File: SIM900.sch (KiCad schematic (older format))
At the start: 72 parts, among them J1 Conn_01x05, J11 Conn_Coaxial_Power, J12 AudioJack2_Ground, J13 AudioJack2_Ground, J2 Conn_01x04, J3 Conn_01x04, J4 Conn_01x06, J5 Conn_01x02, J6 Conn_01x06, J7 Conn_01x03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

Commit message: Se realizaron los cambios a los comentarios hechos por el profesor
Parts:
- C1, C10, C11, C12, C13, C14, C15, C16, C17, C18, C19, C2, C20, C3, C4, C5, C6, C7, C8: Digikey (none) -> 399-17617-2-ND
- C9: Degikey (none) -> 399-17617-2-ND
- D1, D11, D2, D4: Digikey (none) -> SMAJ22CAQ-13-FDITR-ND
- D10, D8, D9: Digikey (none) -> BZD27C16P-E3-08GITR-ND
- D3: Digikey (none) -> 2460-L171L-QYC-TR-ND
- D5: Digokey (none) -> SMAJ22CAQ-13-FDITR-ND
- D6: Digikey (none) -> 2460-L171L-LICTR-ND
- D7: Field4 (none) -> BZD27C16P-E3-08GITR-ND
- J1: Digikey (none) -> S6103-ND
- J11: Digikey (none) -> H9161DKR-ND
- J12, J13: Digikey (none) -> CP-SJ2-35813B-SMT-DKR-ND
- J2, J3: Digikey (none) -> S9009E-04-ND
- J4, J6: Digikey (none) -> S7004-ND
- J7: Digikey (none) -> S9008E-03-ND
- J8: Digikey (none) -> 2057-RF2-49B-T-00-50-G-HDW-ND
- J9: Digikey (none) -> WM6698DKR-ND
- L1: footprint Inductor_SMD:L_0603_1608Metric_Pad1.05x0.95mm_HandSolder -> Inductor_SMD:L_0805_2012Metric; Digikey (none) -> 490-LQW2BAS6N0J00LDKR-ND
- Q1, Q2, Q3: Digikey (none) -> BC848BHZGT116DKR-ND
- R1, R10, R11, R12, R13, R15, R2, R3, R4, R5, R6, R7, R8: Digikey (none) -> 73L3R10JTR-ND
- R9: Degikey (none) -> 73L3R10JTR-ND
- U1: Digikey (none) -> 576-1124-ND
- U2: Digikey (none) -> 1597-1231-ND
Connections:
- net RXD: now also XA1.25 (rs232TXD); no longer XA1.23 (rs232RXD)
- net TXD: now also XA1.23 (rs232RXD); no longer XA1.25 (rs232TXD)

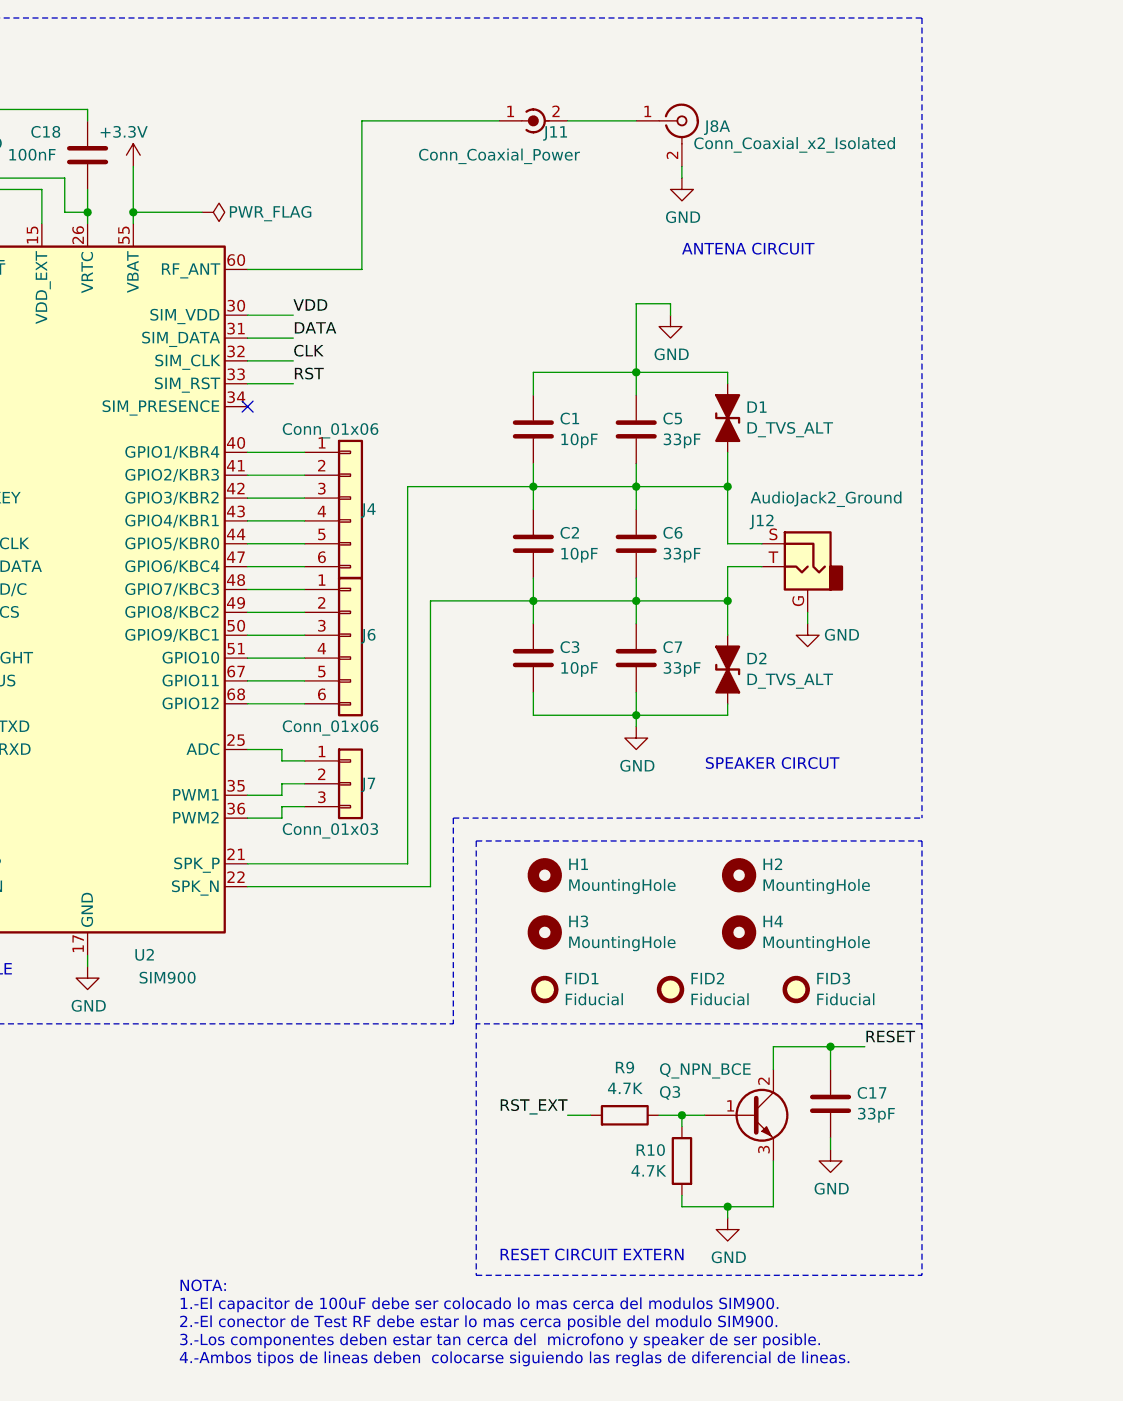
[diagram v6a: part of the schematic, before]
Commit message: Correccion de los comentarios realizados por el profesor al PCB
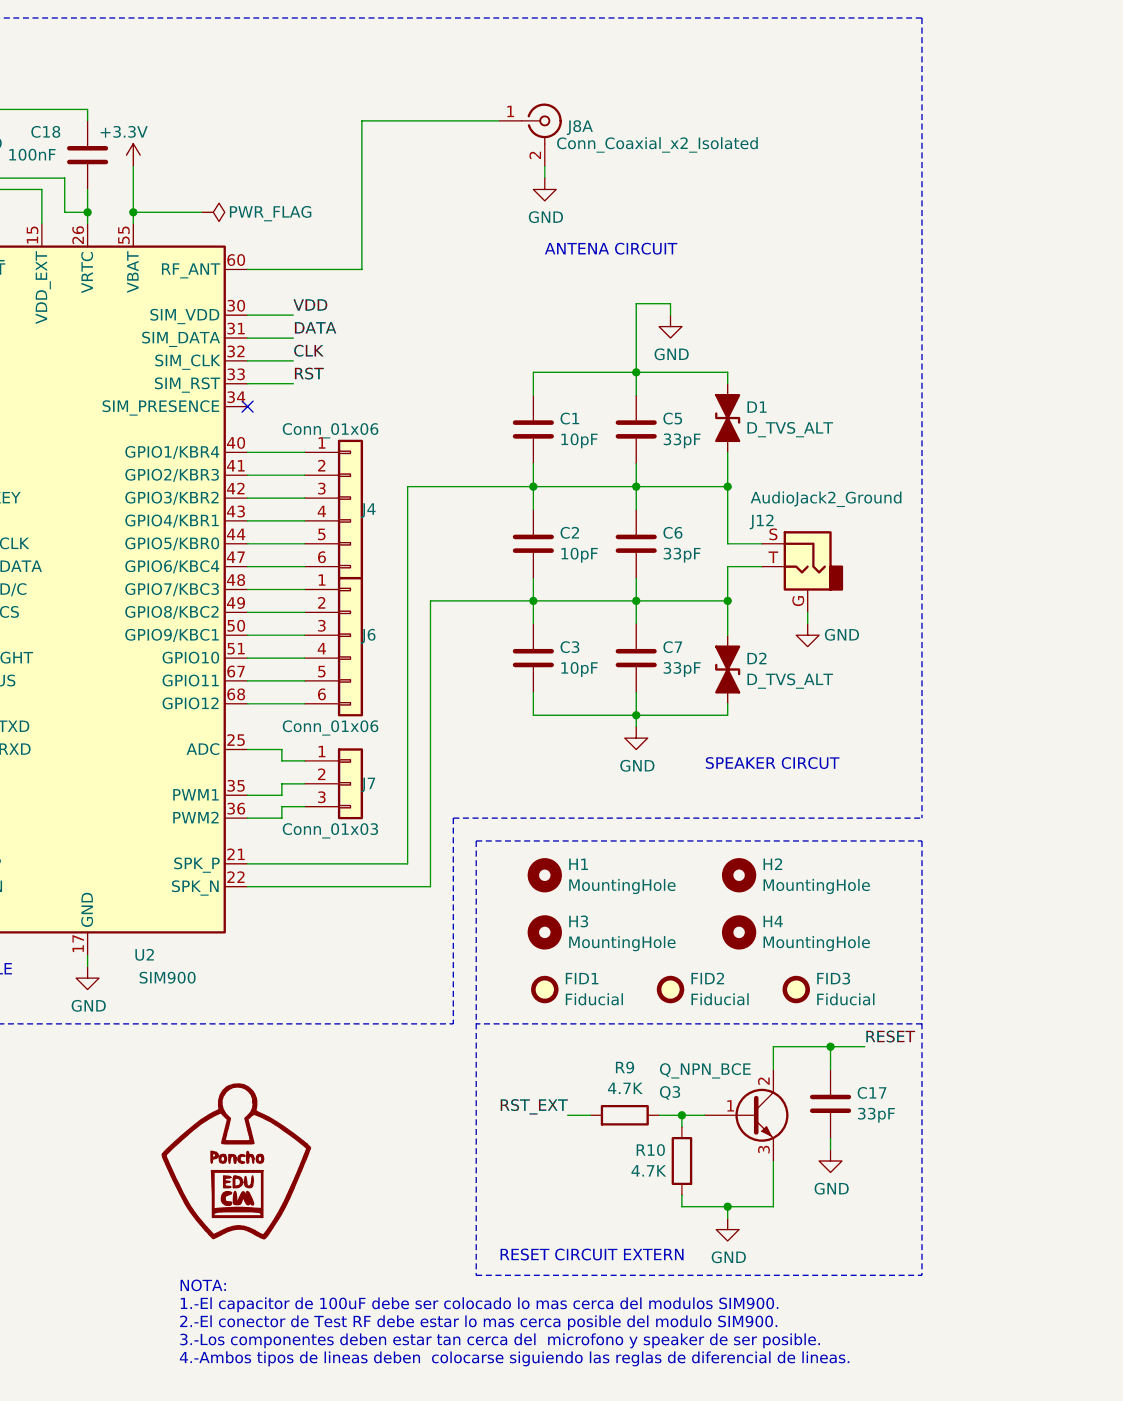
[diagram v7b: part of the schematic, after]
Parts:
- removed J11: Conn_Coaxial_Power, Connector_Coaxial:U.FL_Hirose_U.FL-R-SMT-1_Vertical, symbol Connector:Conn_Coaxial_Power
- C4: footprint Capacitor_SMD:C_0805_2012Metric -> Capacitor_SMD:C_1206_3216Metric; Digikey 399-17617-2-ND -> 718-2364-6-ND
- C9: Degikey 399-17617-2-ND -> 399-3878-6-ND
- J1: footprint Connector_PinHeader_2.00mm:PinHeader_1x05_P2.00mm_Vertical -> Connector_PinHeader_2.54mm:PinHeader_1x05_P2.54mm_Vertical
- J2, J3: footprint Connector_PinHeader_2.00mm:PinHeader_1x04_P2.00mm_Vertical -> Connector_PinHeader_2.54mm:PinHeader_1x04_P2.54mm_Vertical
- J4, J6: footprint Connector_PinHeader_2.00mm:PinHeader_1x06_P2.00mm_Vertical -> Connector_PinHeader_2.54mm:PinHeader_1x06_P2.54mm_Vertical
- J7: footprint Connector_PinHeader_2.00mm:PinHeader_1x03_P2.00mm_Vertical -> Connector_PinHeader_2.54mm:PinHeader_1x03_P2.54mm_Vertical
- J8: footprint Connector_Coaxial:SMA_Amphenol_132203-12_Horizontal -> Connector_Coaxial:SMA_Amphenol_901-144_Vertical
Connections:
- net at U2.60 (RF_ANT): now also J8.1 (In1)
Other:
- moved on the sheet: J8A
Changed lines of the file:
@@
 F 0 "C4" H 1200 1100 50  0000 L CNN
 F 1 "100uF" H 1200 1000 50  0000 L CNN
-F 2 "Capacitor_SMD:C_0805_2012Metric" H 1150 1200 50  0001 C CNN
+F 2 "Capacitor_SMD:C_1206_3216Metric" H 1150 1200 50  0001 C CNN
 F 3 "~" H 1150 1200 50  0001 C CNN
-F 4 "399-17617-2-ND" H 1150 1200 50  0001 C CNN "Digikey"
+F 4 "718-2364-6-ND" H 1150 1200 50  0001 C CNN "Digikey"
 	1    1150 1200
 	1    0    0    -1
@@
 F 2 "Capacitor_SMD:C_0805_2012Metric" H 3800 1200 50  0001 C CNN
 F 3 "~" H 3800 1200 50  0001 C CNN
-F 4 "399-17617-2-ND" H 3800 1200 50  0001 C CNN "Degikey"
+F 4 "399-3878-6-ND" H 3800 1200 50  0001 C CNN "Degikey"
 	1    3800 1200
 	1    0    0    -1
@@
 F 0 "J3" H 6300 3250 50  0000 C CNN
 F 1 "Conn_01x04" H 6000 3200 50  0000 C CNN
-F 2 "Connector_PinHeader_2.00mm:PinHeader_1x04_P2.00mm_Vertical" H 6250 3000 50  0001 C CNN
+F 2 "Connector_PinHeader_2.54mm:PinHeader_1x04_P2.54mm_Vertical" H 6250 3000 50  0001 C CNN
 F 3 "~" H 6250 3000 50  0001 C CNN
 F 4 "S9009E-04-ND" H 6250 3000 50  0001 C CNN "Digikey"
@@
 F 0 "J7" H 8600 3950 50  0000 L CNN
 F 1 "Conn_01x03" H 8250 3750 50  0000 L CNN
-F 2 "Connector_PinHeader_2.00mm:PinHeader_1x03_P2.00mm_Vertical" H 8550 3950 50  0001 C CNN
+F 2 "Connector_PinHeader_2.54mm:PinHeader_1x03_P2.54mm_Vertical" H 8550 3950 50  0001 C CNN
 F 3 "~" H 8550 3950 50  0001 C CNN
 F 4 "S9008E-03-ND" H 8550 3950 50  0001 C CNN "Digikey"
@@
 F 0 "J4" H 8600 2650 50  0000 L CNN
 F 1 "Conn_01x06" H 8250 3000 50  0000 L CNN
-F 2 "Connector_PinHeader_2.00mm:PinHeader_1x06_P2.00mm_Vertical" H 8550 2700 50  0001 C CNN
+F 2 "Connector_PinHeader_2.54mm:PinHeader_1x06_P2.54mm_Vertical" H 8550 2700 50  0001 C CNN
 F 3 "~" H 8550 2700 50  0001 C CNN
 F 4 "S7004-ND" H 8550 2700 50  0001 C CNN "Digikey"
@@
 F 0 "J6" H 8600 3300 50  0000 L CNN
 F 1 "Conn_01x06" H 8250 2900 50  0000 L CNN
-F 2 "Connector_PinHeader_2.00mm:PinHeader_1x06_P2.00mm_Vertical" H 8550 3300 50  0001 C CNN
+F 2 "Connector_PinHeader_2.54mm:PinHeader_1x06_P2.54mm_Vertical" H 8550 3300 50  0001 C CNN
 F 3 "~" H 8550 3300 50  0001 C CNN
 F 4 "S7004-ND" H 8550 3300 50  0001 C CNN "Digikey"
@@
 F 0 "J2" H 6350 4050 50  0000 C CNN
 F 1 "Conn_01x04" H 6050 4000 50  0000 C CNN
-F 2 "Connector_PinHeader_2.00mm:PinHeader_1x04_P2.00mm_Vertical" H 6250 3800 50  0001 C CNN
+F 2 "Connector_PinHeader_2.54mm:PinHeader_1x04_P2.54mm_Vertical" H 6250 3800 50  0001 C CNN
 F 3 "~" H 6250 3800 50  0001 C CNN
 F 4 "S9009E-04-ND" H 6250 3800 50  0001 C CNN "Digikey"
@@
 F 0 "J1" H 6350 2450 50  0000 C CNN
 F 1 "Conn_01x05" H 6050 2400 50  0000 C CNN
-F 2 "Connector_PinHeader_2.00mm:PinHeader_1x05_P2.00mm_Vertical" H 6250 2100 50  0001 C CNN
+F 2 "Connector_PinHeader_2.54mm:PinHeader_1x05_P2.54mm_Vertical" H 6250 2100 50  0001 C CNN
 F 3 "~" H 6250 2100 50  0001 C CNN
 F 4 "S6103-ND" H 6250 2100 50  0001 C CNN "Digikey"
@@
 $EndComp
 Wire Wire Line
-	9800 1050 9500 1050
-$Comp
-L Connector:Conn_Coaxial_Power J11
-U 1 1 5F80D385
-P 9300 1050
-F 0 "J11" V 9250 900 50  0000 C CNN
-F 1 "Conn_Coaxial_Power" V 9150 1150 50  0000 C CNN
-F 2 "Connector_Coaxial:U.FL_Hirose_U.FL-R-SMT-1_Vertical" H 9300 1000 50  0001 C CNN
-F 3 "~" H 9300 1000 50  0001 C CNN
-F 4 "H9161DKR-ND" V 9300 1050 50  0001 C CNN "Digikey"
-	1    9300 1050
-	0    -1   -1   0
-$EndComp
-Wire Wire Line
-	10000 1250 10000 1300
+	9400 1250 9400 1300
 $Comp
 L power:GND #PWR03
 U 1 1 5FE876DE
-P 10000 1300
-F 0 "#PWR03" H 10000 1050 50  0001 C CNN
-F 1 "GND" H 10005 1127 50  0000 C CNN
-F 2 "" H 10000 1300 50  0001 C CNN
-F 3 "" H 10000 1300 50  0001 C CNN
-	1    10000 1300
+P 9400 1300
+F 0 "#PWR03" H 9400 1050 50  0001 C CNN
+F 1 "GND" H 9405 1127 50  0000 C CNN
+F 2 "" H 9400 1300 50  0001 C CNN
+F 3 "" H 9400 1300 50  0001 C CNN
+	1    9400 1300
 	1    0    0    -1
 $EndComp
@@
 L Connector:Conn_Coaxial_x2_Isolated J8
 U 1 1 5FE618B1
-P 10000 1050
-F 0 "J8" H 10100 1025 50  0000 L CNN
-F 1 "Conn_Coaxial_x2_Isolated" H 10050 950 50  0000 L CNN
-F 2 "Connector_Coaxial:SMA_Amphenol_132203-12_Horizontal" H 10000 1050 50  0001 C CNN
-F 3 " ~" H 10000 1050 50  0001 C CNN
-F 4 "2057-RF2-49B-T-00-50-G-HDW-ND" H 10000 1050 50  0001 C CNN "Digikey"
-	1    10000 1050
-	1    0    0    -1
-$EndComp
-Text Notes 10000 1650 0    50   ~ 0
+P 9400 1050
+F 0 "J8" H 9500 1025 50  0000 L CNN
+F 1 "Conn_Coaxial_x2_Isolated" H 9450 950 50  0000 L CNN
+F 2 "Connector_Coaxial:SMA_Amphenol_901-144_Vertical" H 9400 1050 50  0001 C CNN
+F 3 " ~" H 9400 1050 50  0001 C CNN
+F 4 "2057-RF2-49B-T-00-50-G-HDW-ND" H 9400 1050 50  0001 C CNN "Digikey"
+	1    9400 1050
+	1    0    0    -1
+$EndComp
+Text Notes 9400 1650 0    50   ~ 0
 ANTENA CIRCUIT
 Wire Wire Line
@@
 	0    1    -1   0
 $EndComp
+$Comp
+L Poncho_Esqueleto:Logo_Poncho #G1
+U 1 1 5FE04FA0
+P 8050 5600
+F 0 "#G1" H 8000 5200 60  0001 C CNN
+F 1 "Logo_Poncho" H 8250 5200 60  0001 C CNN
+F 2 "" H 8050 5600 60  0000 C CNN
+F 3 "" H 8050 5600 60  0000 C CNN
+	1    8050 5600
+	1    0    0    -1
+$EndComp
 $EndSCHEMATC

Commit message: se corrigio algunas cosas faltantes de las observaciones realizadas
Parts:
- C9: footprint Capacitor_SMD:C_0805_2012Metric -> Footprint:C_2312_2020Metric_Pad3.2x6.0mm_HandSolder
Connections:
- net +5V: now also XA1.2 (+5V); no longer XA1.42 (+5V)
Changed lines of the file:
@@
 F 0 "C9" H 3915 1246 50  0000 L CNN
 F 1 "330uF" H 3915 1155 50  0000 L CNN
-F 2 "Capacitor_SMD:C_0805_2012Metric" H 3800 1200 50  0001 C CNN
+F 2 "Footprint:C_2312_2020Metric_Pad3.2x6.0mm_HandSolder" H 3800 1200 50  0001 C CNN
 F 3 "~" H 3800 1200 50  0001 C CNN
 F 4 "399-3878-6-ND" H 3800 1200 50  0001 C CNN "Degikey"
@@
 NoConn ~ 5300 5500
 Wire Wire Line
-	5000 5500 5050 5500
-Wire Wire Line
-	5050 5500 5050 5450
+	6500 5500 6550 5500
+Wire Wire Line
+	6550 5500 6550 5450
 $Comp
 L Mechanical:MountingHole H2
@@
 	7400 1450 7400 1500
 NoConn ~ 3800 5500
-NoConn ~ 6500 5500
 $Comp
 L power:+5V #PWR0120
 U 1 1 60039D5B
-P 5050 5450
-F 0 "#PWR0120" H 5050 5300 50  0001 C CNN
-F 1 "+5V" H 5065 5623 50  0000 C CNN
-F 2 "" H 5050 5450 50  0001 C CNN
-F 3 "" H 5050 5450 50  0001 C CNN
-	1    5050 5450
+P 6550 5450
+F 0 "#PWR0120" H 6550 5300 50  0001 C CNN
+F 1 "+5V" H 6565 5623 50  0000 C CNN
+F 2 "" H 6550 5450 50  0001 C CNN
+F 3 "" H 6550 5450 50  0001 C CNN
+	1    6550 5450
 	1    0    0    -1
 $EndComp
@@
 L Poncho_Esqueleto:Logo_Poncho #G1
 U 1 1 5FE04FA0
-P 8050 5600
-F 0 "#G1" H 8000 5200 60  0001 C CNN
-F 1 "Logo_Poncho" H 8250 5200 60  0001 C CNN
-F 2 "" H 8050 5600 60  0000 C CNN
-F 3 "" H 8050 5600 60  0000 C CNN
-	1    8050 5600
-	1    0    0    -1
-$EndComp
+P 7450 5550
+F 0 "#G1" H 7400 5150 60  0001 C CNN
+F 1 "Logo_Poncho" H 7650 5150 60  0001 C CNN
+F 2 "" H 7450 5550 60  0000 C CNN
+F 3 "" H 7450 5550 60  0000 C CNN
+	1    7450 5550
+	1    0    0    -1
+$EndComp
+NoConn ~ 5000 5500
+$Comp
+L Poncho_Esqueleto:OSHWA #G?
+U 1 1 5FB8E829
+P 8300 5500
+F 0 "#G?" H 8270 5900 60  0001 C CNN
+F 1 "OSHWA" H 8300 5803 60  0001 C CNN
+F 2 "" H 8300 5500 60  0000 C CNN
+F 3 "" H 8300 5500 60  0000 C CNN
+	1    8300 5500
+	1    0    0    -1
+$EndComp
